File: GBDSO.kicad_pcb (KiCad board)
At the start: 2 copper layers, 85 x 61 mm, 77 parts, among them J1 MJ-3523-SMT-TR, J2 MJ-3523-SMT-TR, J3 EdgeConnector, J4 GameBoy Cartridge Connector, J5 Conn_01x02, J6 Conn_01x02, P1 100k, P2 100k, SW1 SW_SPDT, SW2 SW_SPDT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

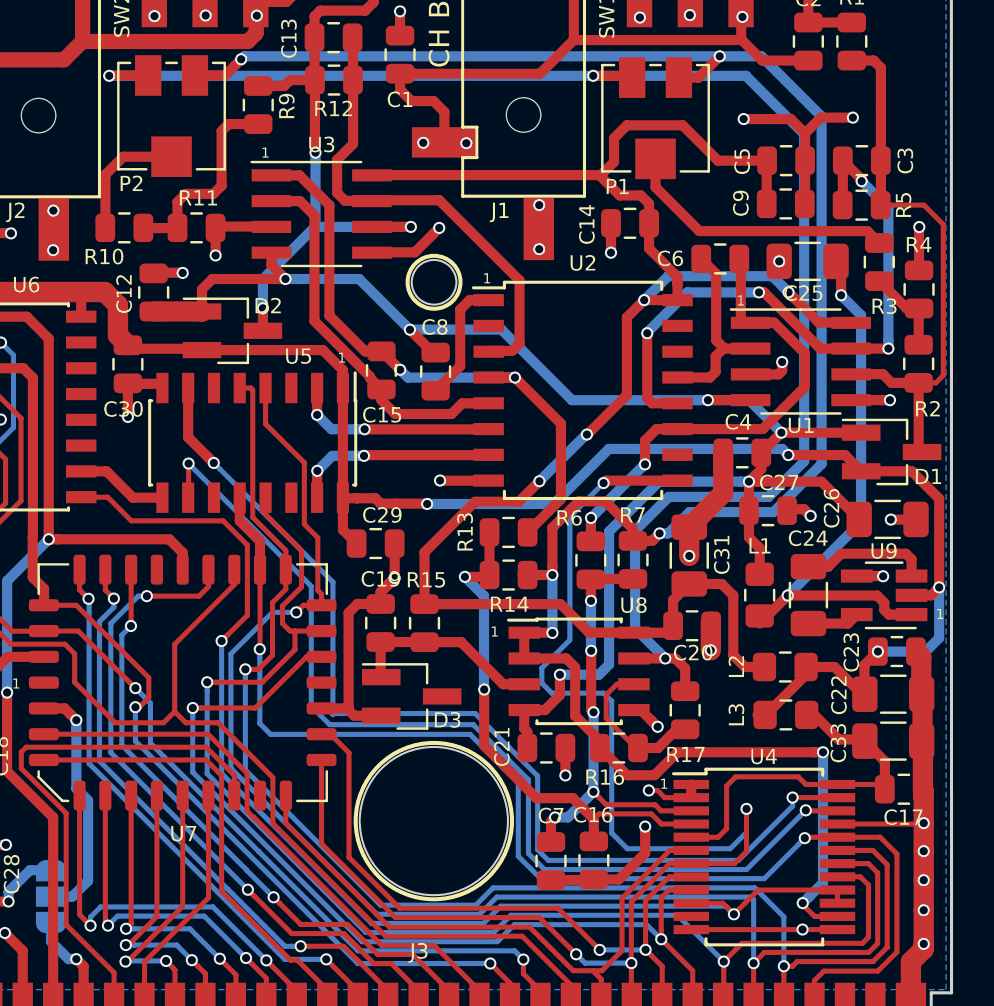
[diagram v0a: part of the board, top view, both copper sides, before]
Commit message: fix #16, fix #17, fix #18 in schematic and PCB
fixed issues #16,  #17, #18 in schematic and PCB, with improvement here and there.
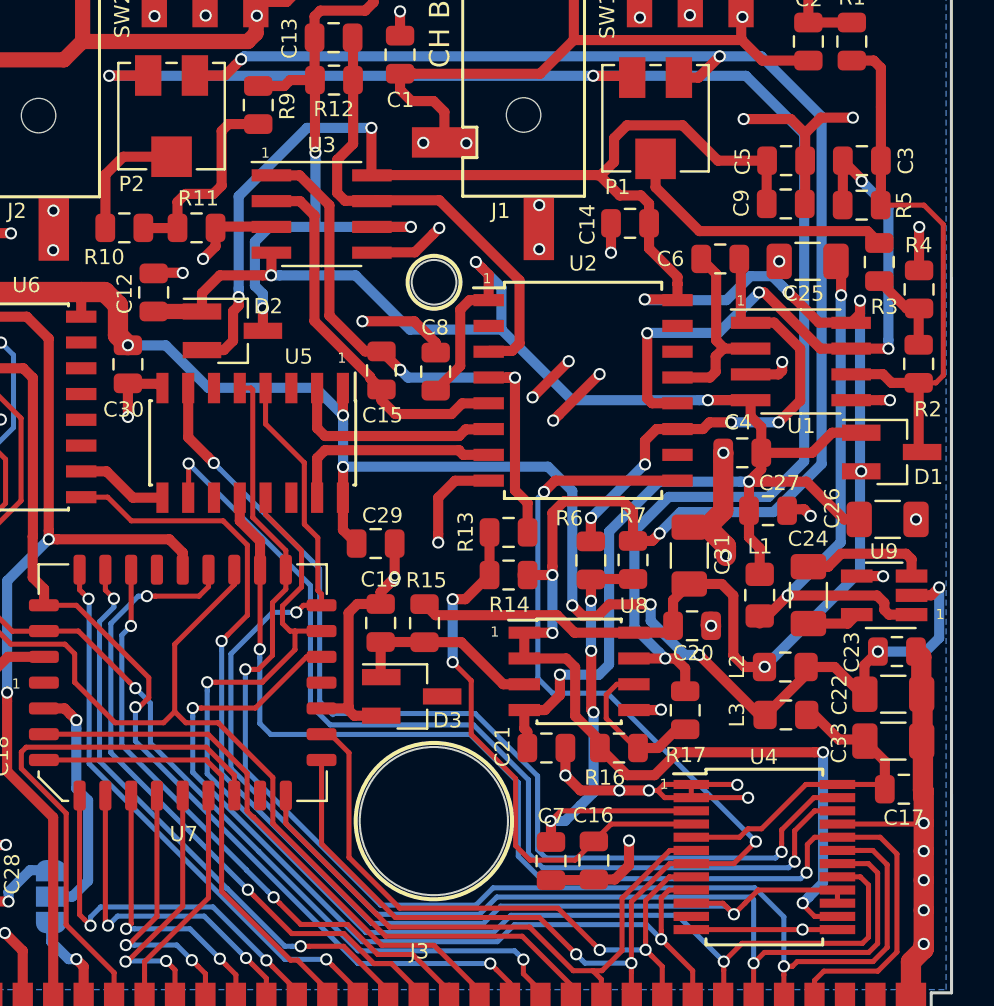
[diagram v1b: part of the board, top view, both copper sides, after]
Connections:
- SW1 pad 3: Net-(SW1-Pad3) -> GND
- SW2 pad 3: Net-(SW2-Pad3) -> GND
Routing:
- net GND: track 189.3 -> 211.3 mm, vias 38 -> 51
- net +5VA: track 88.5 -> 108.4 mm, vias 4 -> 7
- net +5V: track 136.2 -> 130.3 mm, vias 5 -> 9
- net /GBDSO Cartridge/D1: track 71.6 -> 66.8 mm
- net -5V: track 86.6 -> 90.7 mm, vias 6 -> 5
- net Net-(C7-Pad1): track 21.3 -> 23.3 mm, vias 5 -> 4
- net Net-(C16-Pad1): track 25.7 -> 27.5 mm
- net Net-(C13-Pad1): track 30.0 -> 31.6 mm
- net +5VC: track 18.1 -> 16.6 mm
- net Net-(C15-Pad1): track 30.9 -> 29.5 mm
- net +2.5V: track 106.7 -> 107.6 mm
- net Net-(U2-Pad7): track 9.87 -> 10.7 mm, vias 2 -> 0
- net Net-(C25-Pad1): track 27.1 -> 26.3 mm
- net /GBDSO Cartridge/D7: track 62.4 -> 63.2 mm
- net Net-(U4-Pad22): track 48.8 -> 49.5 mm
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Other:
- rule trace_min: 0.12 -> 0.1

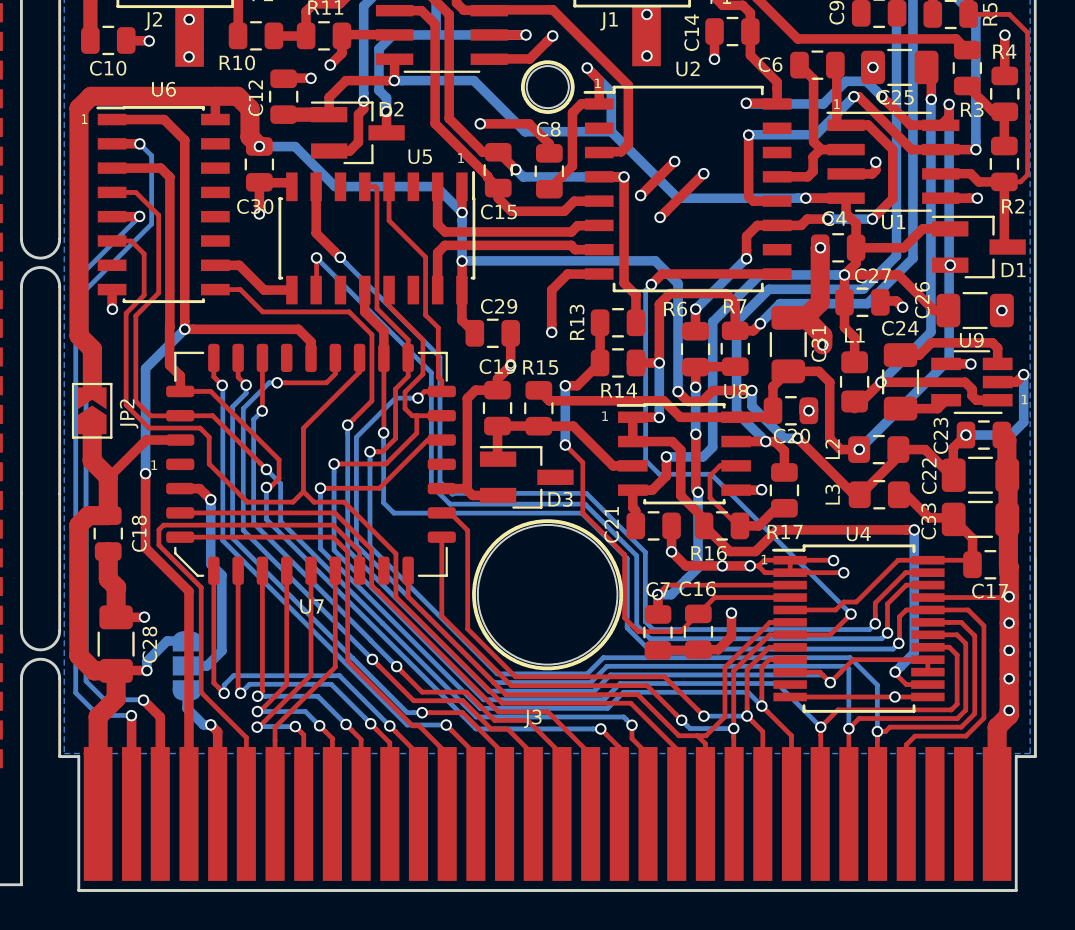
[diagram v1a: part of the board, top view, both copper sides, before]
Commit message: Used the new PLCC32 handsolder footprint and moved a few traces around
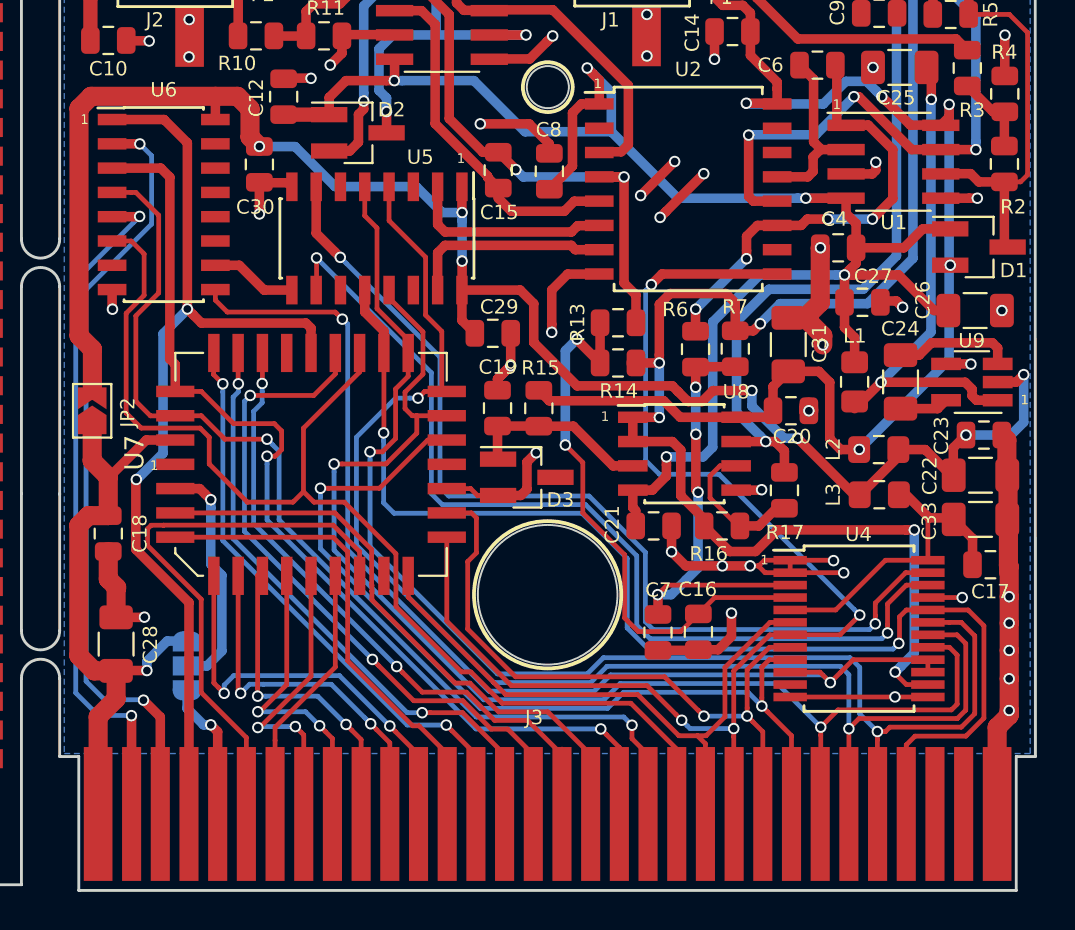
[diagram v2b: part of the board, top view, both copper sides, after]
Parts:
- U7: footprint Package_LCC:PLCC-32_11.4x14.0mm_P1.27mm -> PLCC32_HandSolder:PLCC-32_HandSolder
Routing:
- net GND: track 211.3 -> 205.9 mm, vias 51 -> 53
- net +5V: track 130.3 -> 127.5 mm, vias 9 -> 8
- net Net-(C16-Pad1): track 27.5 -> 29.6 mm
- net /GBDSO Cartridge/A13: track 51.6 -> 52.9 mm
- net /GBDSO Cartridge/~RD: track 48.9 -> 50.1 mm
- net Net-(U4-Pad10): track 58.3 -> 57.2 mm
- net /GBDSO Cartridge/A14: track 52.2 -> 53.1 mm
- net /GBDSO Cartridge/A0: track 28.8 -> 29.7 mm
- net /GBDSO Cartridge/D1: track 66.8 -> 67.6 mm
- net /GBDSO Cartridge/D2: track 33.9 -> 34.7 mm
- net /GBDSO Cartridge/A15: track 60.6 -> 61.1 mm

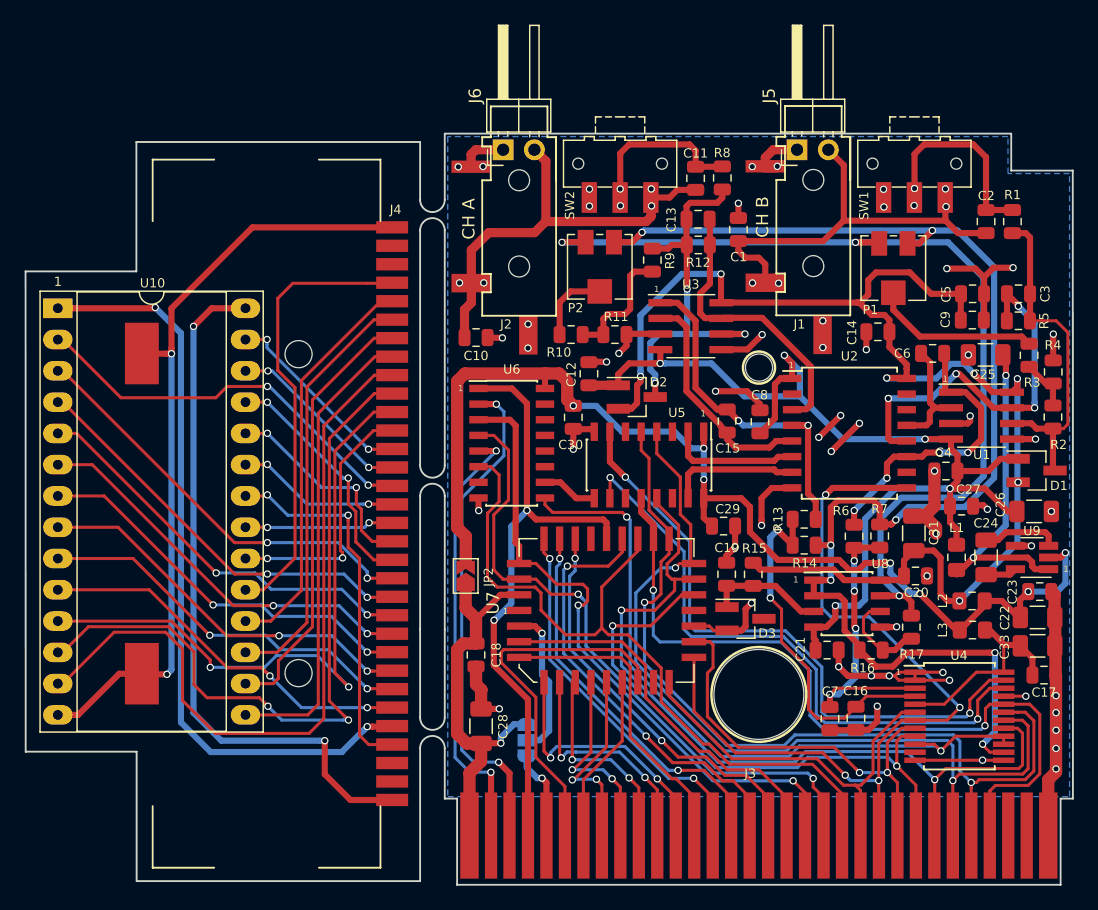
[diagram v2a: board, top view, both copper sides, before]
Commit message: added some art and fixed the resistors R3-R4/R10-R11
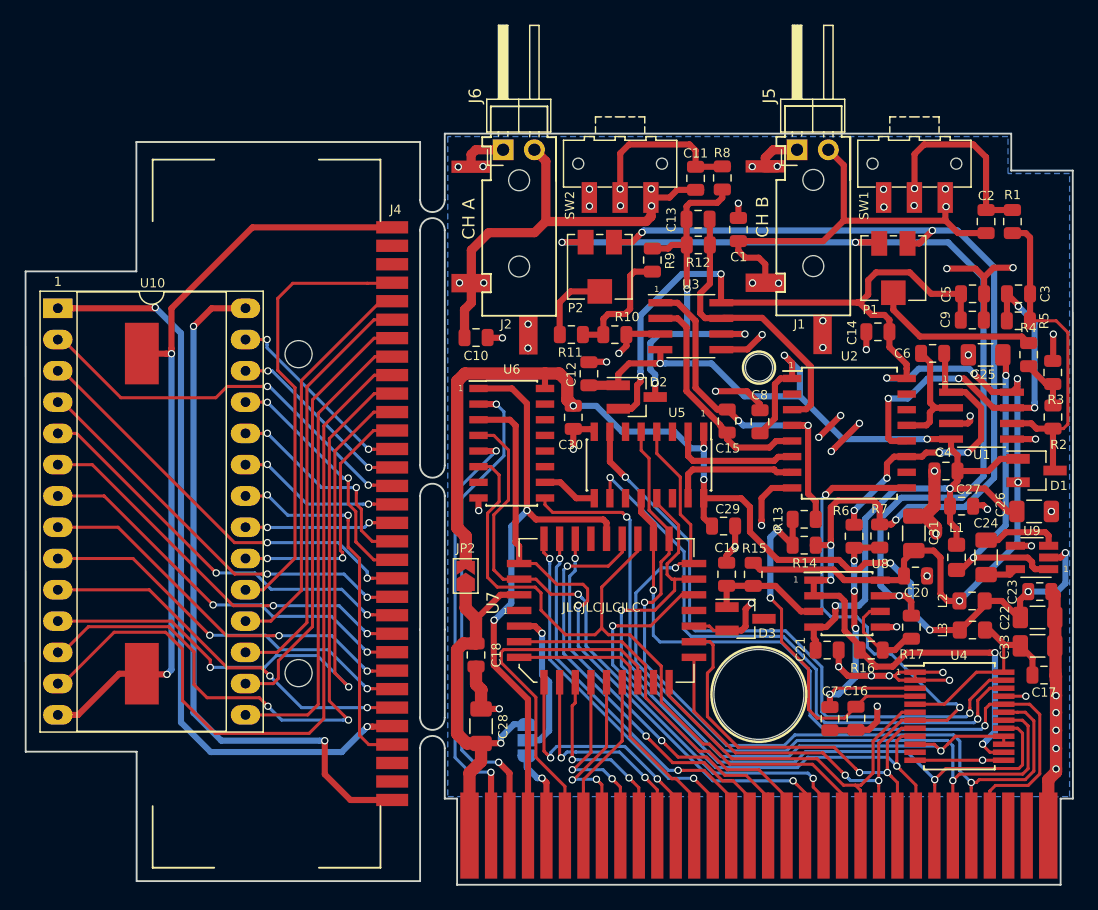
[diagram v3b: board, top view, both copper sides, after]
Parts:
- added G***: LOGO, art:space_invader, B.Cu at (163.8, 100.3)
- moved R10 3.55 mm to (152.2, 86.0), turned to 180 degrees
- moved R11 3.54 mm to (148.7, 86.0), turned to 0 degrees
- moved R4 2.44 mm to (185.8, 87.6)
- moved R3 2.37 mm to (187.8, 89.0)
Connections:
- R10 pad 1: Net-(P2-Pad2) -> GND
- R11 pad 1: GND -> Net-(P2-Pad2)
- R3 pad 1: Net-(P1-Pad2) -> GND
- R4 pad 1: GND -> Net-(P1-Pad2)
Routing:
- net Net-(J1-Pad10): track 0.00 -> 2.17 mm
- net Net-(C1-Pad1): track 37.2 -> 39.3 mm
- net Net-(C10-Pad1): track 37.6 -> 39.6 mm
- net Net-(J2-Pad10): track 0.00 -> 1.95 mm
- net -5V: track 90.7 -> 88.9 mm
- net Net-(C2-Pad2): track 16.2 -> 17.6 mm
- net Net-(C11-Pad1): track 13.9 -> 15.2 mm
- net /GBDSO Cartridge/D1: track 67.6 -> 68.5 mm
- net +5V: track 127.5 -> 128.4 mm
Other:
- rule pad_to_mask_clearance: 0.2 -> 0
- board text added: "JLCJLCJLCJLC"
